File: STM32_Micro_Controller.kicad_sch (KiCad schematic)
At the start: 1 part, among them U1 STM32F103C8T6

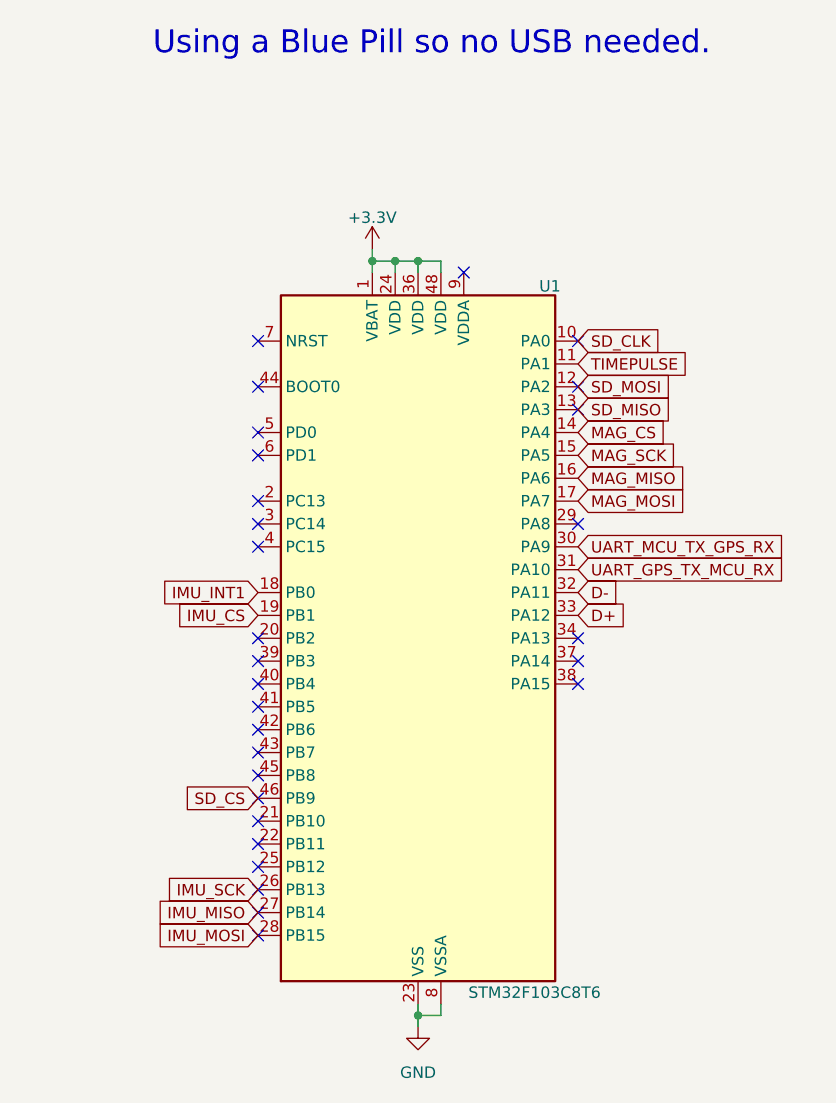
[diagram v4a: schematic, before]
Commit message: Fixed the second round of issues Sam gave us
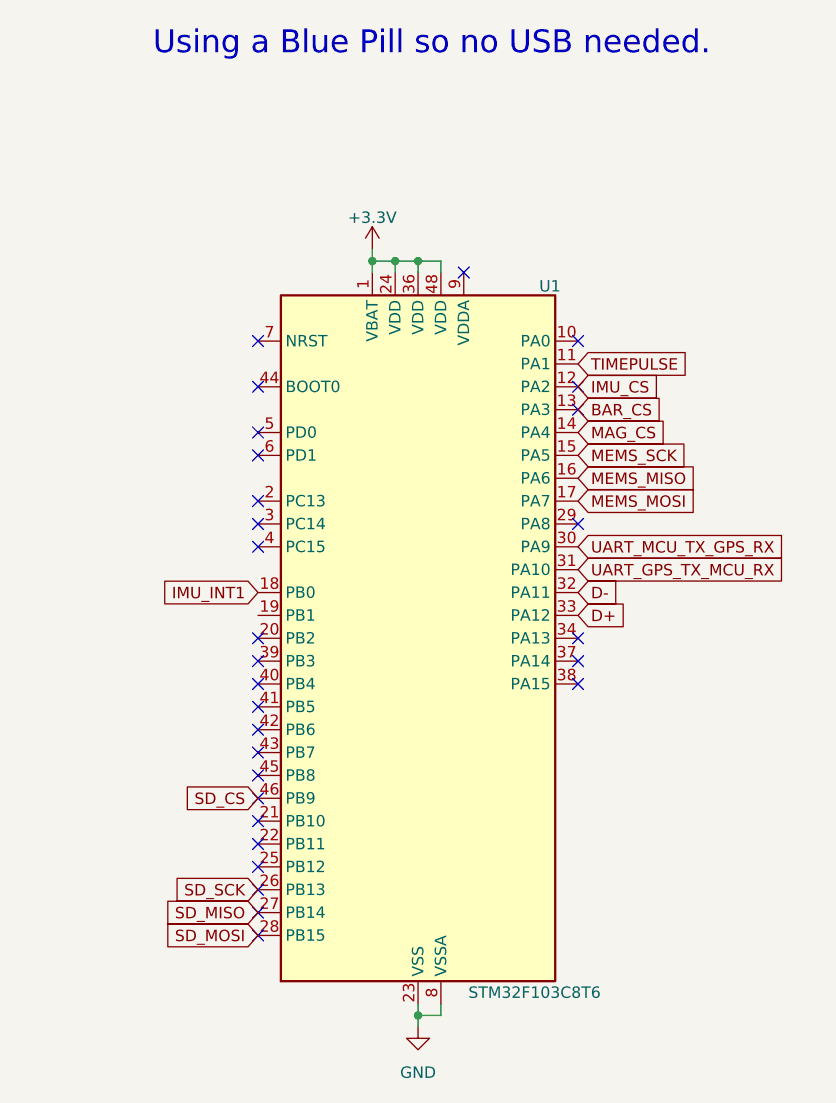
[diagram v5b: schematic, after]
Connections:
- net IMU_MISO is gone; now on net SD_MISO: U1.27 (PB14)
- net IMU_MOSI is gone; now on net SD_MOSI: U1.28 (PB15)
- net IMU_CS: now also U1.12 (PA2); no longer U1.19 (PB1)
- net SD_MISO: no longer U1.13 (PA3)
- net SD_MOSI: no longer U1.12 (PA2)
- net IMU_SCK renamed SD_SCK
- net MAG_MISO renamed MEMS_MISO
- net MAG_MOSI renamed MEMS_MOSI
- net MAG_SCK renamed MEMS_SCK
- net SD_CLK: no longer names the net of U1.10 (PA0)
- new net BAR_CS: U1.13 (PA3)
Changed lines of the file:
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@@
 		)
 	)
-	(global_label "MAG_SCK"
+	(global_label "MEMS_SCK"
 		(shape input)
 		(at 148.59 72.39 0)
@@
 		)
 		(property "Intersheetrefs" "${INTERSHEET_REFS}"
-			(at 160.1023 72.39 0)
+			(at 161.5536 72.39 0)
 			(effects
 				(font
@@
 		)
 	)
+	(global_label "BAR_CS"
+		(shape input)
+		(at 148.59 67.31 0)
+		(fields_autoplaced yes)
+		(effects
+			(font
+				(size 1.27 1.27)
+			)
+			(justify left)
+		)
+		(property "Intersheetrefs" "${INTERSHEET_REFS}"
+			(at 158.6509 67.31 0)
+			(effects
+				(font
+					(size 1.27 1.27)
+				)
+				(justify left)
+				(hide yes)
+			)
+		)
+	)
 	(global_label "SD_CS"
 		(shape input)
@@
 		)
 	)
-	(global_label "IMU_MISO"
+	(global_label "IMU_INT1"
+		(shape input)
+		(at 113.03 87.63 180)
+		(fields_autoplaced yes)
+		(effects
+			(font
+				(size 1.27 1.27)
+			)
+			(justify right)
+		)
+		(property "Intersheetrefs" "${INTERSHEET_REFS}"
+			(at 101.5781 87.63 0)
+			(effects
+				(font
+					(size 1.27 1.27)
+				)
+				(justify right)
+				(hide yes)
+			)
+		)
+	)
+	(global_label "D-"
+		(shape input)
+		(at 148.59 87.63 0)
+		(fields_autoplaced yes)
+		(effects
+			(font
+				(size 1.27 1.27)
+			)
+			(justify left)
+		)
+		(property "Intersheetrefs" "${INTERSHEET_REFS}"
+			(at 154.4176 87.63 0)
+			(effects
+				(font
+					(size 1.27 1.27)
+				)
+				(justify left)
+				(hide yes)
+			)
+		)
+	)
+	(global_label "UART_MCU_TX_GPS_RX"
+		(shape input)
+		(at 148.59 82.55 0)
+		(fields_autoplaced yes)
+		(effects
+			(font
+				(size 1.27 1.27)
+			)
+			(justify left)
+		)
+		(property "Intersheetrefs" "${INTERSHEET_REFS}"
+			(at 172.5603 82.55 0)
+			(effects
+				(font
+					(size 1.27 1.27)
+				)
+				(justify left)
+				(hide yes)
+			)
+		)
+	)
+	(global_label "MEMS_MISO"
+		(shape input)
+		(at 148.59 74.93 0)
+		(fields_autoplaced yes)
+		(effects
+			(font
+				(size 1.27 1.27)
+			)
+			(justify left)
+		)
+		(property "Intersheetrefs" "${INTERSHEET_REFS}"
+			(at 162.4003 74.93 0)
+			(effects
+				(font
+					(size 1.27 1.27)
+				)
+				(justify left)
+				(hide yes)
+			)
+		)
+	)
+	(global_label "IMU_CS"
+		(shape input)
+		(at 148.59 64.77 0)
+		(fields_autoplaced yes)
+		(effects
+			(font
+				(size 1.27 1.27)
+			)
+			(justify left)
+		)
+		(property "Intersheetrefs" "${INTERSHEET_REFS}"
+			(at 158.409 64.77 0)
+			(effects
+				(font
+					(size 1.27 1.27)
+				)
+				(justify left)
+				(hide yes)
+			)
+		)
+	)
+	(global_label "SD_MISO"
 		(shape input)
 		(at 113.03 123.19 180)
@@
 		)
 		(property "Intersheetrefs" "${INTERSHEET_REFS}"
-			(at 101.0943 123.19 0)
-			(effects
-				(font
-					(size 1.27 1.27)
-				)
-				(justify right)
-				(hide yes)
-			)
-		)
-	)
-	(global_label "IMU_INT1"
-		(shape input)
-		(at 113.03 87.63 180)
-		(fields_autoplaced yes)
-		(effects
-			(font
-				(size 1.27 1.27)
-			)
-			(justify right)
-		)
-		(property "Intersheetrefs" "${INTERSHEET_REFS}"
-			(at 101.5781 87.63 0)
-			(effects
-				(font
-					(size 1.27 1.27)
-				)
-				(justify right)
-				(hide yes)
-			)
-		)
-	)
-	(global_label "D-"
-		(shape input)
-		(at 148.59 87.63 0)
-		(fields_autoplaced yes)
-		(effects
-			(font
-				(size 1.27 1.27)
-			)
-			(justify left)
-		)
-		(property "Intersheetrefs" "${INTERSHEET_REFS}"
-			(at 154.4176 87.63 0)
-			(effects
-				(font
-					(size 1.27 1.27)
-				)
-				(justify left)
-				(hide yes)
-			)
-		)
-	)
-	(global_label "UART_MCU_TX_GPS_RX"
-		(shape input)
-		(at 148.59 82.55 0)
-		(fields_autoplaced yes)
-		(effects
-			(font
-				(size 1.27 1.27)
-			)
-			(justify left)
-		)
-		(property "Intersheetrefs" "${INTERSHEET_REFS}"
-			(at 172.5603 82.55 0)
-			(effects
-				(font
-					(size 1.27 1.27)
-				)
-				(justify left)
-				(hide yes)
-			)
-		)
-	)
-	(global_label "MAG_MISO"
-		(shape input)
-		(at 148.59 74.93 0)
-		(fields_autoplaced yes)
-		(effects
-			(font
-				(size 1.27 1.27)
-			)
-			(justify left)
-		)
-		(property "Intersheetrefs" "${INTERSHEET_REFS}"
-			(at 160.949 74.93 0)
-			(effects
-				(font
-					(size 1.27 1.27)
-				)
-				(justify left)
+			(at 102.0015 123.19 0)
+			(effects
+				(font
+					(size 1.27 1.27)
+				)
+				(justify right)
 				(hide yes)
 			)
@@
 		)
 	)
-	(global_label "SD_CLK"
-		(shape input)
-		(at 148.59 59.69 0)
-		(fields_autoplaced yes)
-		(effects
-			(font
-				(size 1.27 1.27)
-			)
-			(justify left)
-		)
-		(property "Intersheetrefs" "${INTERSHEET_REFS}"
-			(at 158.5904 59.69 0)
-			(effects
-				(font
-					(size 1.27 1.27)
-				)
-				(justify left)
-				(hide yes)
-			)
-		)
-	)
-	(global_label "IMU_MOSI"
+	(global_label "SD_MOSI"
 		(shape input)
 		(at 113.03 125.73 180)
@@
 		)
 		(property "Intersheetrefs" "${INTERSHEET_REFS}"
-			(at 101.0943 125.73 0)
-			(effects
-				(font
-					(size 1.27 1.27)
-				)
-				(justify right)
-				(hide yes)
-			)
-		)
-	)
-	(global_label "SD_MISO"
-		(shape input)
-		(at 148.59 67.31 0)
-		(fields_autoplaced yes)
-		(effects
-			(font
-				(size 1.27 1.27)
-			)
-			(justify left)
-		)
-		(property "Intersheetrefs" "${INTERSHEET_REFS}"
-			(at 159.6185 67.31 0)
-			(effects
-				(font
-					(size 1.27 1.27)
-				)
-				(justify left)
-				(hide yes)
-			)
-		)
-	)
-	(global_label "SD_MOSI"
-		(shape input)
-		(at 148.59 64.77 0)
-		(fields_autoplaced yes)
-		(effects
-			(font
-				(size 1.27 1.27)
-			)
-			(justify left)
-		)
-		(property "Intersheetrefs" "${INTERSHEET_REFS}"
-			(at 159.6185 64.77 0)
-			(effects
-				(font
-					(size 1.27 1.27)
-				)
-				(justify left)
+			(at 102.0015 125.73 0)
+			(effects
+				(font
+					(size 1.27 1.27)
+				)
+				(justify right)
+				(hide yes)
+			)
+		)
+	)
+	(global_label "SD_SCK"
+		(shape input)
+		(at 113.03 120.65 180)
+		(fields_autoplaced yes)
+		(effects
+			(font
+				(size 1.27 1.27)
+			)
+			(justify right)
+		)
+		(property "Intersheetrefs" "${INTERSHEET_REFS}"
+			(at 102.8482 120.65 0)
+			(effects
+				(font
+					(size 1.27 1.27)
+				)
+				(justify right)
 				(hide yes)
 			)
@@
 		)
 	)
-	(global_label "IMU_CS"
-		(shape input)
-		(at 113.03 90.17 180)
-		(fields_autoplaced yes)
-		(effects
-			(font
-				(size 1.27 1.27)
-			)
-			(justify right)
-		)
-		(property "Intersheetrefs" "${INTERSHEET_REFS}"
-			(at 103.211 90.17 0)
-			(effects
-				(font
-					(size 1.27 1.27)
-				)
-				(justify right)
-				(hide yes)
-			)
-		)
-	)
-	(global_label "IMU_SCK"
-		(shape input)
-		(at 113.03 120.65 180)
-		(fields_autoplaced yes)
-		(effects
-			(font
-				(size 1.27 1.27)
-			)
-			(justify right)
-		)
-		(property "Intersheetrefs" "${INTERSHEET_REFS}"
-			(at 101.941 120.65 0)
-			(effects
-				(font
-					(size 1.27 1.27)
-				)
-				(justify right)
-				(hide yes)
-			)
-		)
-	)
-	(global_label "MAG_MOSI"
+	(global_label "MEMS_MOSI"
 		(shape input)
 		(at 148.59 77.47 0)
@@
 		)
 		(property "Intersheetrefs" "${INTERSHEET_REFS}"
-			(at 160.949 77.47 0)
-			(effects
-				(font
+			(at 162.4003 77.47 0)
+			(effects
+				(font

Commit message: Updated the STM32 footprint
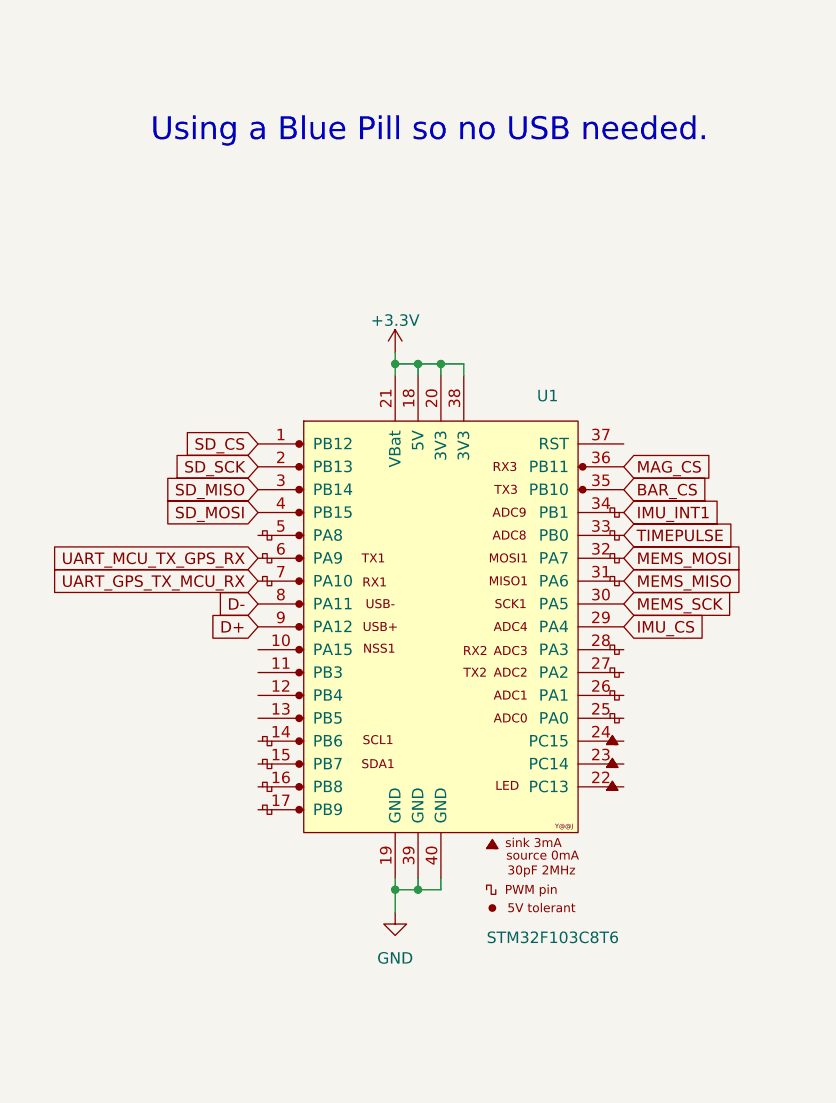
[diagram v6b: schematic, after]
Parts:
- U1: symbol MCU_ST_STM32F1:STM32F103C8Tx -> YAAJ_BluePill:YAAJ_BluePill
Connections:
- net +3.3V: now also U1.18 (5V), U1.20 (3V3), U1.21 (VBat), U1.38 (3V3); no longer U1.1 (VBAT), U1.24 (VDD), U1.36 (VDD), U1.48 (VDD)
- net BAR_CS: now also U1.35 (PB10); no longer U1.13 (PA3)
- net D+: now also U1.9 (PA12); no longer U1.33 (PA12)
- net D-: now also U1.8 (PA11); no longer U1.32 (PA11)
- net GND: now also U1.19 (GND), U1.39 (GND), U1.40 (GND); no longer U1.23 (VSS), U1.35 (VSS), U1.47 (VSS), U1.8 (VSSA)
- net IMU_CS: now also U1.29 (PA4); no longer U1.12 (PA2)
- net IMU_INT1: now also U1.34 (PB1); no longer U1.18 (PB0)
- net MAG_CS: now also U1.36 (PB11); no longer U1.14 (PA4)
- net MEMS_MISO: now also U1.31 (PA6); no longer U1.16 (PA6)
- net MEMS_MOSI: now also U1.32 (PA7); no longer U1.17 (PA7)
- net MEMS_SCK: now also U1.30 (PA5); no longer U1.15 (PA5)
- net SD_CS: now also U1.1 (PB12); no longer U1.46 (PB9)
- net SD_MISO: now also U1.3 (PB14); no longer U1.27 (PB14)
- net SD_MOSI: now also U1.4 (PB15); no longer U1.28 (PB15)
- net SD_SCK: now also U1.2 (PB13); no longer U1.26 (PB13)
- net TIMEPULSE: now also U1.33 (PB0); no longer U1.11 (PA1)
- net UART_GPS_TX_MCU_RX: now also U1.7 (PA10); no longer U1.31 (PA10)
- net UART_MCU_TX_GPS_RX: now also U1.6 (PA9); no longer U1.30 (PA9)
- no-connect marks 29 -> 0
